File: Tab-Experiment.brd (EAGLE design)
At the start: 95 x 25 mm, 24 parts, among them J1 2X6-HEADERS, J2 95501-6889VERT, U2 ATSAMD09, U3 M24C02-WMN6TP, U4 PCA9615

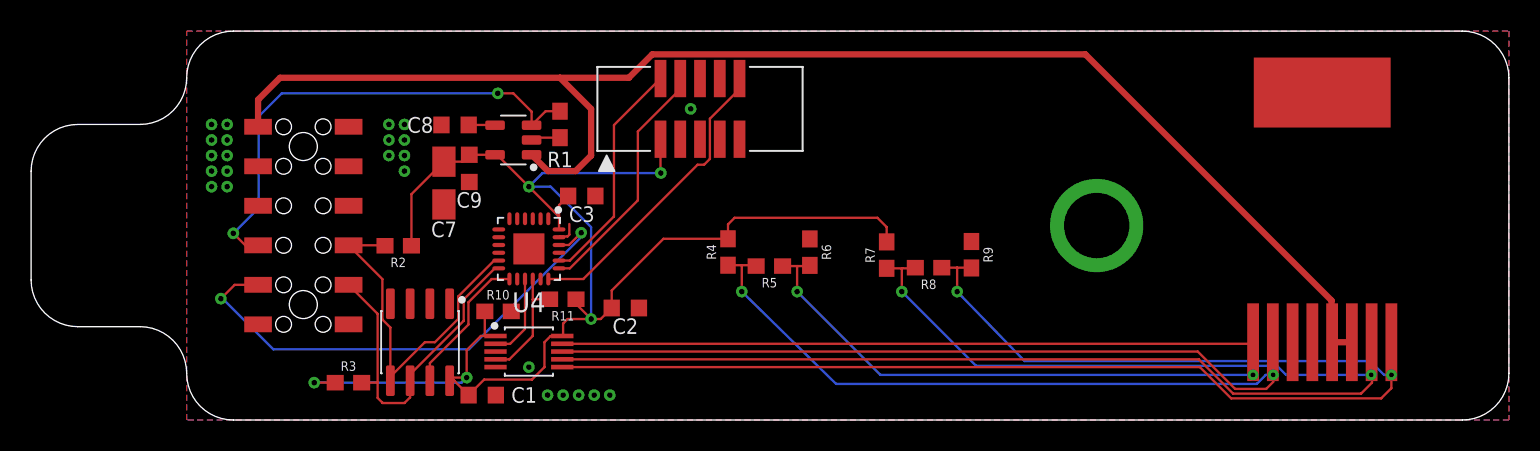
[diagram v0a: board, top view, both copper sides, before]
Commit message: Fixed pullups and mfg cleanup.
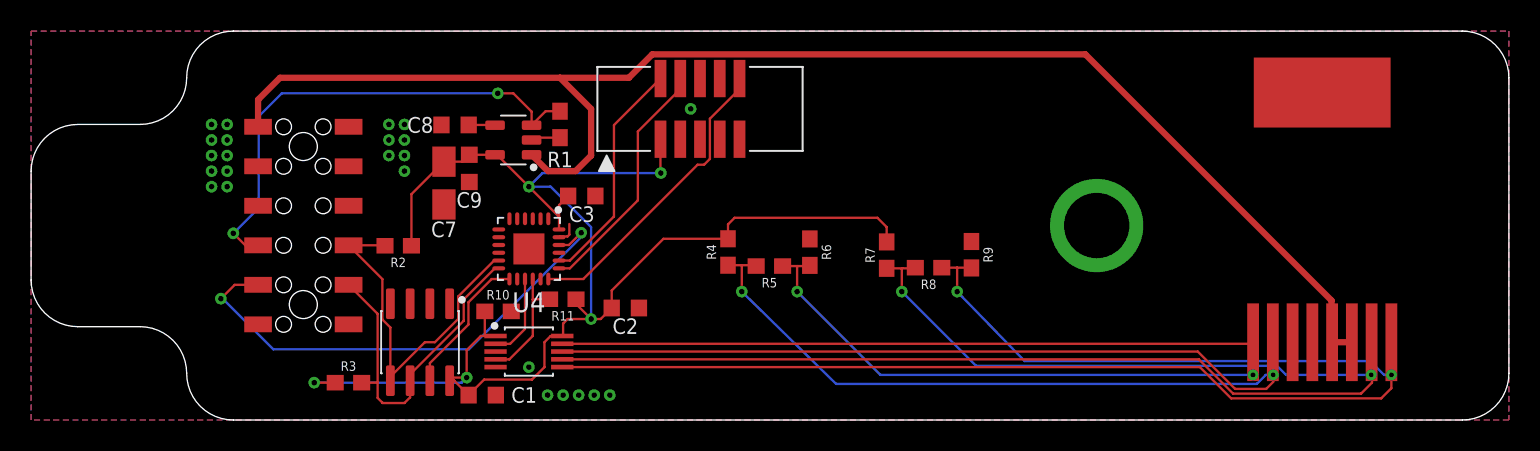
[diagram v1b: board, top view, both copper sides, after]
